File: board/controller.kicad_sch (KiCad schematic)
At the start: 26 parts, among them U1 W5500, Y1 25MHz

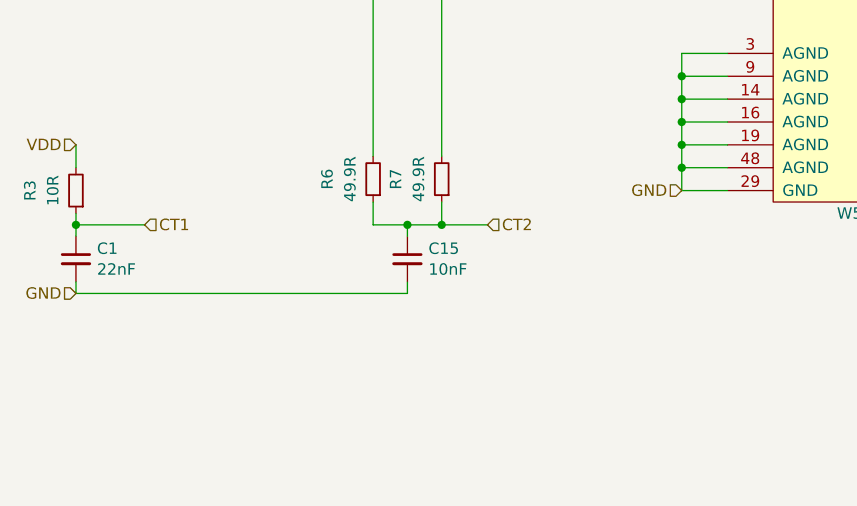
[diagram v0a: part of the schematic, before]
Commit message: added option for shorted center taps
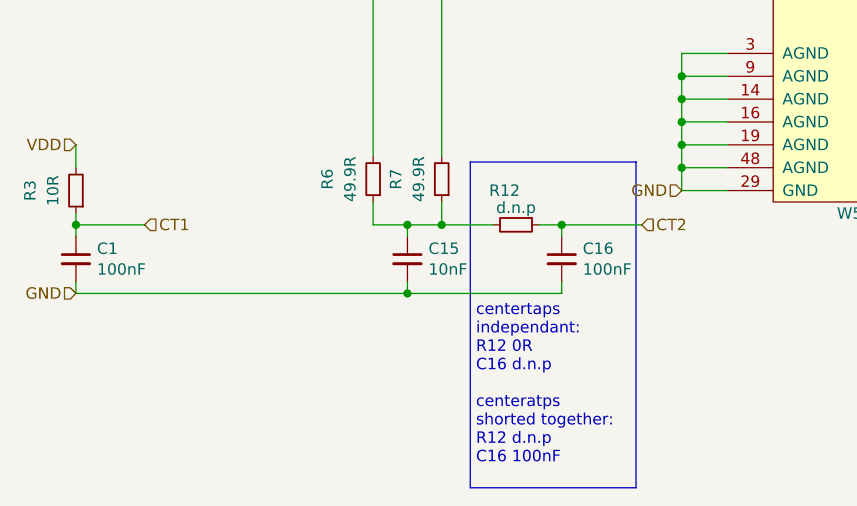
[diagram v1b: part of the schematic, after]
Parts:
- added C16: 100nF, Capacitor_SMD:C_0603_1608Metric, symbol Device:C_Small
- added R12: d.n.p, Resistor_SMD:R_0805_2012Metric, symbol Device:R_Small
- C1: value 22nF -> 100nF
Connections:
- net CT2: now also C16.1, R12.1; no longer C15.1, R6.1, R7.1
- net GND: now also C16.2
- new net: C15.1, R12.2, R6.1, R7.1
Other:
- note added: "centertaps independant: R12 0R C16 d.n.p centeratps shorted together: R12 d.n.p C16 100nF"
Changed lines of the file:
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@@
   (junction (at 62.23 92.71) (diameter 0) (color 0 0 0 0)
   )
+  (junction (at 92.71 129.54) (diameter 0) (color 0 0 0 0)
+  )
   (junction (at 189.23 116.84) (diameter 0) (color 0 0 0 0)
   )
@@
   )
   (junction (at 162.56 110.49) (diameter 0) (color 0 0 0 0)
+  )
+  (junction (at 109.855 121.92) (diameter 0) (color 0 0 0 0)
   )
   (junction (at 95.25 50.8) (diameter 0) (color 0 0 0 0)
@@
     (stroke (width 0) (type default) (color 0 0 0 0))
   )
+  (polyline (pts (xy 118.11 114.935) (xy 99.695 114.935))
+    (stroke (width 0) (type default) (color 0 0 0 0))
+  )
   (wire (pts (xy 92.71 121.92) (xy 92.71 123.19))
     (stroke (width 0) (type default) (color 0 0 0 0))
@@
     (stroke (width 0) (type default) (color 0 0 0 0))
   )
+  (polyline (pts (xy 99.695 151.13) (xy 118.11 151.13))
+    (stroke (width 0) (type default) (color 0 0 0 0))
+  )
   (wire (pts (xy 105.41 57.15) (xy 105.41 54.61))
     (stroke (width 0) (type default) (color 0 0 0 0))
@@
     (stroke (width 0) (type default) (color 0 0 0 0))
   )
-  (wire (pts (xy 96.52 121.92) (xy 101.6 121.92))
+  (wire (pts (xy 96.52 121.92) (xy 102.235 121.92))
     (stroke (width 0) (type default) (color 0 0 0 0))
   )
@@
     (stroke (width 0) (type default) (color 0 0 0 0))
   )
+  (wire (pts (xy 92.71 129.54) (xy 109.855 129.54))
+    (stroke (width 0) (type default) (color 0 0 0 0))
+  )
   (wire (pts (xy 158.75 107.95) (xy 162.56 107.95))
     (stroke (width 0) (type default) (color 0 0 0 0))
@@
     (stroke (width 0) (type default) (color 0 0 0 0))
   )
+  (polyline (pts (xy 99.695 114.935) (xy 99.695 151.13))
+    (stroke (width 0) (type default) (color 0 0 0 0))
+  )
   (wire (pts (xy 92.71 129.54) (xy 92.71 128.27))
     (stroke (width 0) (type default) (color 0 0 0 0))
@@
     (stroke (width 0) (type default) (color 0 0 0 0))
   )
+  (polyline (pts (xy 118.11 114.935) (xy 118.11 151.13))
+    (stroke (width 0) (type default) (color 0 0 0 0))
+  )
   (wire (pts (xy 87.63 64.77) (xy 80.01 64.77))
     (stroke (width 0) (type default) (color 0 0 0 0))
@@
     (stroke (width 0) (type default) (color 0 0 0 0))
   )
+  (wire (pts (xy 109.855 129.54) (xy 109.855 128.27))
+    (stroke (width 0) (type default) (color 0 0 0 0))
+  )
   (wire (pts (xy 83.82 90.17) (xy 88.9 90.17))
     (stroke (width 0) (type default) (color 0 0 0 0))
@@
     (stroke (width 0) (type default) (color 0 0 0 0))
   )
+  (wire (pts (xy 118.745 121.92) (xy 109.855 121.92))
+    (stroke (width 0) (type default) (color 0 0 0 0))
+  )
   (wire (pts (xy 125.73 92.71) (xy 128.27 92.71))
     (stroke (width 0) (type default) (color 0 0 0 0))
@@
     (stroke (width 0) (type default) (color 0 0 0 0))
   )
+  (wire (pts (xy 109.855 121.92) (xy 109.855 123.19))
+    (stroke (width 0) (type default) (color 0 0 0 0))
+  )
   (wire (pts (xy 162.56 38.1) (xy 162.56 44.45))
     (stroke (width 0) (type default) (color 0 0 0 0))
@@
     (stroke (width 0) (type default) (color 0 0 0 0))
   )
+  (wire (pts (xy 107.315 121.92) (xy 109.855 121.92))
+    (stroke (width 0) (type default) (color 0 0 0 0))
+  )
   (wire (pts (xy 58.42 92.71) (xy 62.23 92.71))
     (stroke (width 0) (type default) (color 0 0 0 0))
@@
   (wire (pts (xy 128.27 52.07) (xy 105.41 52.07))
     (stroke (width 0) (type default) (color 0 0 0 0))
+  )
+  (text "centertaps \nindependant:\nR12 0R\nC16 d.n.p\n\ncenteratps\nshorted together:\nR12 d.n.p\nC16 100nF"
+    (at 100.33 148.59 0)
+    (effects (font (size 1.27 1.27)) (justify left bottom))
   )
   (label "XCAP" (at 160.02 97.79 0)
@@
     (effects (font (size 1.27 1.27)) (justify right))
   )
-  (hierarchical_label "CT2" (shape input) (at 101.6 121.92 0)
+  (hierarchical_label "CT2" (shape input) (at 118.745 121.92 0)
     (effects (font (size 1.27 1.27)) (justify left))
   )
@@
   (hierarchical_label "INT" (shape input) (at 190.5 64.77 0)
     (effects (font (size 1.27 1.27)) (justify left))
+  )
+  (symbol (lib_id "Device:R_Small") (at 104.775 121.92 270) (unit 1)
+    (in_bom yes) (on_board yes)
+    (property "Reference" "R12" (id 0) (at 103.505 118.11 90))
+    (property "Value" "d.n.p" (id 1) (at 104.775 120.015 90))
+    (property "Footprint" "Resistor_SMD:R_0805_2012Metric" (id 2) (at 104.775 121.92 0)
+      (effects (font (size 1.27 1.27)) hide)
+    )
+    (property "Datasheet" "~" (id 3) (at 104.775 121.92 0)
+      (effects (font (size 1.27 1.27)) hide)
+    )
+    (pin "1")
+    (pin "2")
   )
   (symbol (lib_id "Device:C_Small") (at 95.25 58.42 0) (unit 1)
@@
     )
     (property "DigiKey Part Number" "1276-1012-1-ND" (id 4) (at 80.01 58.42 0)
+      (effects (font (size 1.27 1.27)) hide)
+    )
+    (pin "1")
+    (pin "2")
+  )
+  (symbol (lib_id "Device:C_Small") (at 109.855 125.73 0) (unit 1)
+    (in_bom yes) (on_board yes)
+    (property "Reference" "C16" (id 0) (at 112.1918 124.5616 0)
+      (effects (font (size 1.27 1.27)) (justify left))
+    )
+    (property "Value" "100nF" (id 1) (at 112.1918 126.873 0)
+      (effects (font (size 1.27 1.27)) (justify left))
+    )
+    (property "Footprint" "Capacitor_SMD:C_0603_1608Metric" (id 2) (at 109.855 125.73 0)
+      (effects (font (size 1.27 1.27)) hide)
+    )
+    (property "Datasheet" "~" (id 3) (at 109.855 125.73 0)
+      (effects (font (size 1.27 1.27)) hide)
+    )
+    (property "Voltage" "6.3V" (id 4) (at 109.855 125.73 0)
       (effects (font (size 1.27 1.27)) hide)
     )
@@
       (effects (font (size 1.27 1.27)) (justify left))
     )
-    (property "Value" "22nF" (id 1) (at 58.2168 126.873 0)
-      (effects (font (size 1.27 1.27)) (justify left))
-    )
+    (property "Value" "100nF" (id 1) (at 58.2168 126.873 0)
+      (effects (font (size 1.27 1.27)) (justify left))
+    )
